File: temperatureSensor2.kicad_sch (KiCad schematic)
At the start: 3 parts, among them J2 Conn_01x03_Pin

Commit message: first draft
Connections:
- net tempSensor1_OUT renamed tempSensor2_OUT
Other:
- note added: "Temperature Sensor 2"
- note removed: "Temperature Sensor 1"

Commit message: revision
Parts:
- added TP2: TestPoint, TestPoint:TestPoint_THTPad_D2.0mm_Drill1.0mm, symbol Connector:TestPoint
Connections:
- net tempSensor2_OUT: now also TP2.1
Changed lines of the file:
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@@
+    )
+  )
+  (symbol (lib_id "Connector:TestPoint") (at 114.3 67.31 0) (unit 1)
+    (in_bom yes) (on_board yes) (dnp no) (fields_autoplaced)
+    (property "Reference" "TP2" (at 116.84 62.738 0)
+      (effects (font (size 1.27 1.27)) (justify left))
+    )
+    (property "Value" "TestPoint" (at 116.84 65.278 0)
+      (effects (font (size 1.27 1.27)) (justify left))
+    )
+    (property "Footprint" "TestPoint:TestPoint_THTPad_D2.0mm_Drill1.0mm" (at 119.38 67.31 0)
+      (effects (font (size 1.27 1.27)) hide)
+    )
+    (property "Datasheet" "~" (at 119.38 67.31 0)
+      (effects (font (size 1.27 1.27)) hide)
+    )
+    (pin "1")
+    (instances
+      (project "Telemetry-Peripheral-SOM-Daughterboard-IMU"
+        (path "/637f68f0-cb9c-412a-8573-5d8e7ef6d8a2/77daee33-11f8-432f-a415-017f7b28dc11"
+          (reference "TP2") (unit 1)
+        )
+      )
     )
   )

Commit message: Integrated changes made by BPS
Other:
- moved on the sheet: C7, C8, J2, TP2

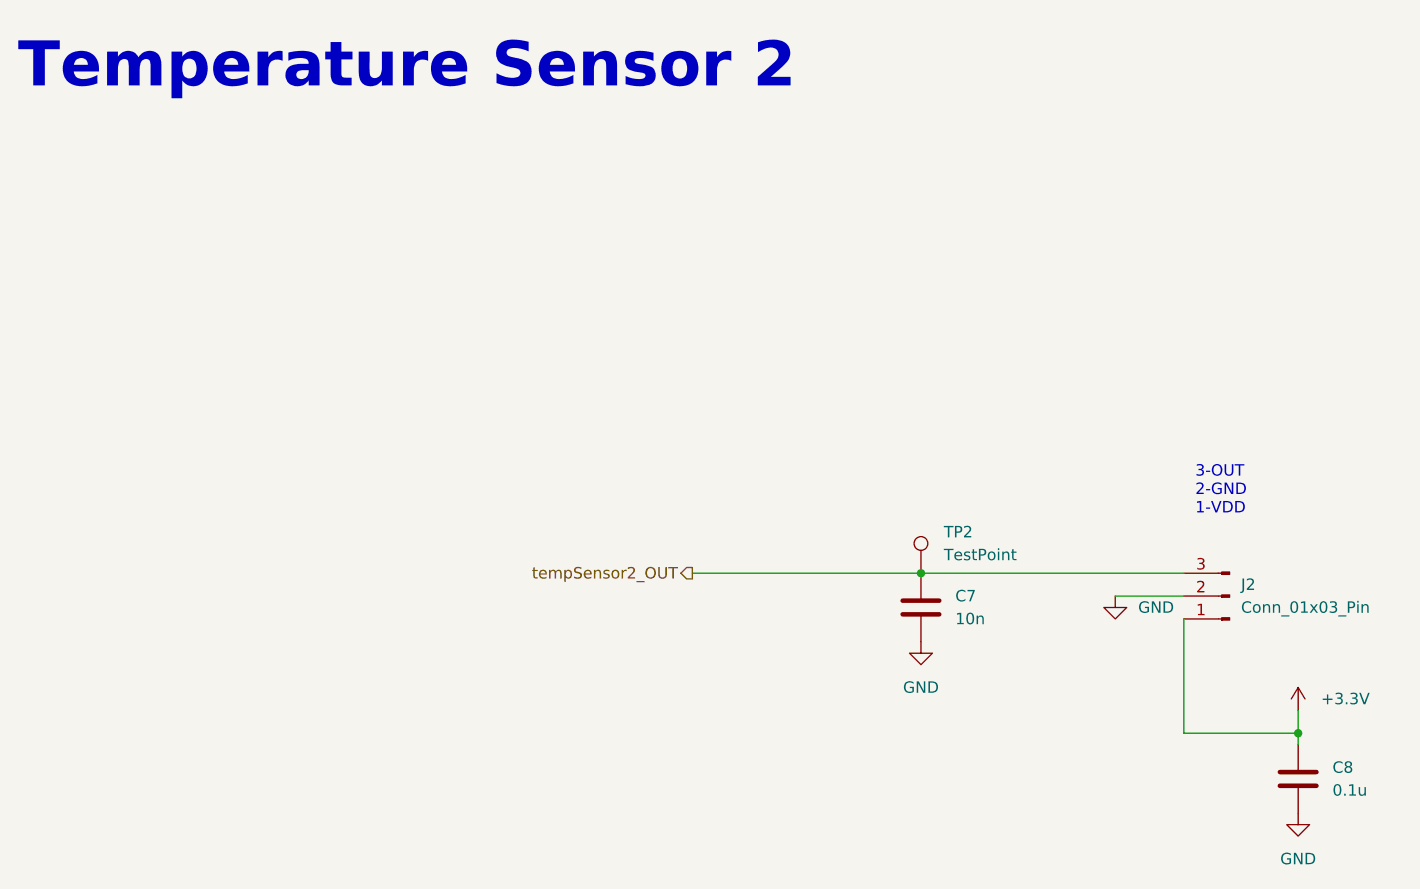
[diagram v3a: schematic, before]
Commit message: added protective circuitry for temp sensors, made name changes for IMU
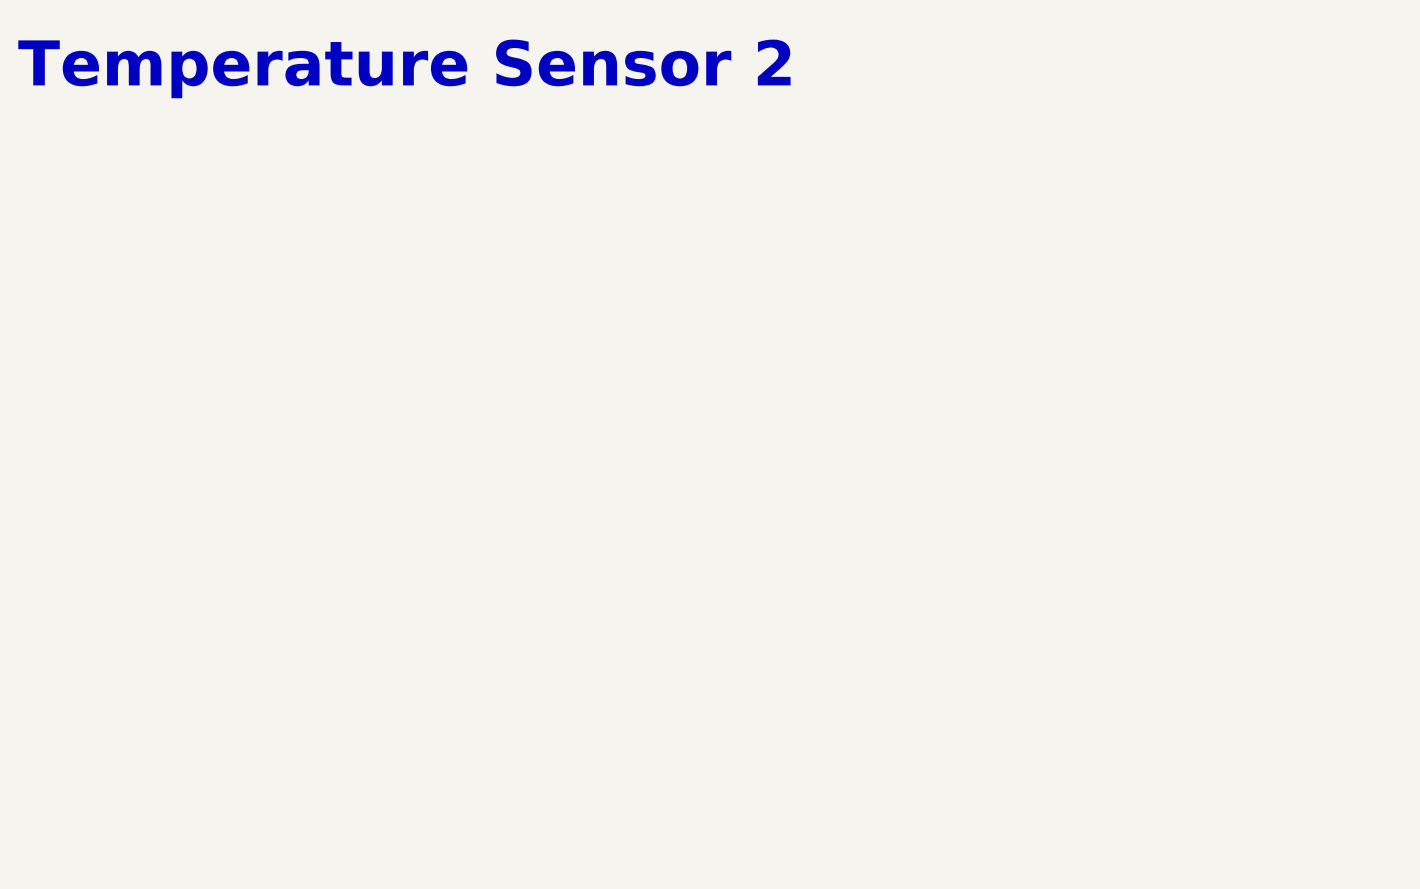
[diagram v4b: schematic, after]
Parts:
- removed C7: 10n, Capacitor_SMD:C_0805_2012Metric, symbol Device:C
- removed C8: 0.1u, Capacitor_SMD:C_0805_2012Metric, symbol Device:C
- removed J2: Conn_01x03_Pin, UTSVT_Connectors:Molex_MicroFit3.0_1x3xP3.00mm_PolarizingPeg_Vertical, symbol Connector:Conn_01x03_Pin
- removed TP2: TestPoint, TestPoint:TestPoint_THTPad_D2.0mm_Drill1.0mm, symbol Connector:TestPoint
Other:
- note removed: "3-OUT 2-GND 1-VDD"
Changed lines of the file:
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@@
 (kicad_sch (version 20230121) (generator eeschema)
   (paper "A4")
-  (junction (at 157.48 92.71) (diameter 0) (color 0 0 0 0)
-  )
-  (junction (at 115.57 74.93) (diameter 0) (color 0 0 0 0)
-  )
-  (wire (pts (xy 115.57 74.93) (xy 144.78 74.93))
-    (stroke (width 0) (type default))
-  )
-  (wire (pts (xy 157.48 92.71) (xy 157.48 93.98))
-    (stroke (width 0) (type default))
-  )
-  (wire (pts (xy 144.78 92.71) (xy 157.48 92.71))
-    (stroke (width 0) (type default))
-  )
-  (wire (pts (xy 157.48 90.17) (xy 157.48 92.71))
-    (stroke (width 0) (type default))
-  )
-  (wire (pts (xy 137.16 77.47) (xy 144.78 77.47))
-    (stroke (width 0) (type default))
-  )
-  (wire (pts (xy 144.78 80.01) (xy 144.78 92.71))
-    (stroke (width 0) (type default))
-  )
-  (wire (pts (xy 90.17 74.93) (xy 115.57 74.93))
-    (stroke (width 0) (type default))
-  )
-  (text "3-OUT\n2-GND\n1-VDD" (at 146.05 68.58 0)
-    (effects (font (size 1.27 1.27)) (justify left bottom))
-  )
   (text "Temperature Sensor 2\n" (at 15.24 21.59 0)
     (effects (font (size 5 5) (thickness 1) bold) (justify left bottom))
   )
-  (hierarchical_label "tempSensor2_OUT" (shape output) (at 90.17 74.93 180) (fields_autoplaced)
-    (effects (font (size 1.27 1.27)) (justify right))
-  )
-  (symbol (lib_id "power:GND") (at 115.57 82.55 0) (unit 1)
-    (in_bom yes) (on_board yes) (dnp no) (fields_autoplaced)
-    (property "Reference" "#PWR017" (at 115.57 88.9 0)
-      (effects (font (size 1.27 1.27)) hide)
-    )
-    (property "Value" "GND" (at 115.57 87.63 0)
-      (effects (font (size 1.27 1.27)))
-    )
-    (property "Footprint" "" (at 115.57 82.55 0)
-      (effects (font (size 1.27 1.27)) hide)
-    )
-    (property "Datasheet" "" (at 115.57 82.55 0)
-      (effects (font (size 1.27 1.27)) hide)
-    )
-    (pin "1")
-    (instances
-      (project "Telemetry-Peripheral-SOM-Daughterboard-IMU"
-        (path "/637f68f0-cb9c-412a-8573-5d8e7ef6d8a2/0366cb5e-31c7-40b1-9d0c-97ad688b48f0"
-          (reference "#PWR017") (unit 1)
-        )
-        (path "/637f68f0-cb9c-412a-8573-5d8e7ef6d8a2/77daee33-11f8-432f-a415-017f7b28dc11"
-          (reference "#PWR04") (unit 1)
-        )
-      )
-    )
-  )
-  (symbol (lib_id "power:GND") (at 157.48 101.6 0) (unit 1)
-    (in_bom yes) (on_board yes) (dnp no) (fields_autoplaced)
-    (property "Reference" "#PWR018" (at 157.48 107.95 0)
-      (effects (font (size 1.27 1.27)) hide)
-    )
-    (property "Value" "GND" (at 157.48 106.68 0)
-      (effects (font (size 1.27 1.27)))
-    )
-    (property "Footprint" "" (at 157.48 101.6 0)
-      (effects (font (size 1.27 1.27)) hide)
-    )
-    (property "Datasheet" "" (at 157.48 101.6 0)
-      (effects (font (size 1.27 1.27)) hide)
-    )
-    (pin "1")
-    (instances
-      (project "Telemetry-Peripheral-SOM-Daughterboard-IMU"
-        (path "/637f68f0-cb9c-412a-8573-5d8e7ef6d8a2/0366cb5e-31c7-40b1-9d0c-97ad688b48f0"
-          (reference "#PWR018") (unit 1)
-        )
-        (path "/637f68f0-cb9c-412a-8573-5d8e7ef6d8a2/77daee33-11f8-432f-a415-017f7b28dc11"
-          (reference "#PWR011") (unit 1)
-        )
-      )
-    )
-  )
-  (symbol (lib_id "Device:C") (at 115.57 78.74 0) (unit 1)
-    (in_bom yes) (on_board yes) (dnp no) (fields_autoplaced)
-    (property "Reference" "C7" (at 119.38 77.47 0)
-      (effects (font (size 1.27 1.27)) (justify left))
-    )
-    (property "Value" "10n" (at 119.38 80.01 0)
-      (effects (font (size 1.27 1.27)) (justify left))
-    )
-    (property "Footprint" "Capacitor_SMD:C_0805_2012Metric" (at 116.5352 82.55 0)
-      (effects (font (size 1.27 1.27)) hide)
-    )
-    (property "Datasheet" "~" (at 115.57 78.74 0)
-      (effects (font (size 1.27 1.27)) hide)
-    )
-    (pin "1")
-    (pin "2")
-    (instances
-      (project "Telemetry-Peripheral-SOM-Daughterboard-IMU"
-        (path "/637f68f0-cb9c-412a-8573-5d8e7ef6d8a2/0366cb5e-31c7-40b1-9d0c-97ad688b48f0"
-          (reference "C7") (unit 1)
-        )
-        (path "/637f68f0-cb9c-412a-8573-5d8e7ef6d8a2/77daee33-11f8-432f-a415-017f7b28dc11"
-          (reference "C9") (unit 1)
-        )
-      )
-    )
-  )
-  (symbol (lib_id "Connector:TestPoint") (at 115.57 74.93 0) (unit 1)
-    (in_bom yes) (on_board yes) (dnp no) (fields_autoplaced)
-    (property "Reference" "TP2" (at 118.11 70.358 0)
-      (effects (font (size 1.27 1.27)) (justify left))
-    )
-    (property "Value" "TestPoint" (at 118.11 72.898 0)
-      (effects (font (size 1.27 1.27)) (justify left))
-    )
-    (property "Footprint" "TestPoint:TestPoint_THTPad_D2.0mm_Drill1.0mm" (at 120.65 74.93 0)
-      (effects (font (size 1.27 1.27)) hide)
-    )
-    (property "Datasheet" "~" (at 120.65 74.93 0)
-      (effects (font (size 1.27 1.27)) hide)
-    )
-    (pin "1")
-    (instances
-      (project "Telemetry-Peripheral-SOM-Daughterboard-IMU"
-        (path "/637f68f0-cb9c-412a-8573-5d8e7ef6d8a2/77daee33-11f8-432f-a415-017f7b28dc11"
-          (reference "TP2") (unit 1)
-        )
-      )
-    )
-  )
-  (symbol (lib_id "power:GND") (at 137.16 77.47 0) (unit 1)
-    (in_bom yes) (on_board yes) (dnp no) (fields_autoplaced)
-    (property "Reference" "#PWR015" (at 137.16 83.82 0)
-      (effects (font (size 1.27 1.27)) hide)
-    )
-    (property "Value" "GND" (at 139.7 78.74 0)
-      (effects (font (size 1.27 1.27)) (justify left))
-    )
-    (property "Footprint" "" (at 137.16 77.47 0)
-      (effects (font (size 1.27 1.27)) hide)
-    )
-    (property "Datasheet" "" (at 137.16 77.47 0)
-      (effects (font (size 1.27 1.27)) hide)
-    )
-    (pin "1")
-    (instances
-      (project "Telemetry-Peripheral-SOM-Daughterboard-IMU"
-        (path "/637f68f0-cb9c-412a-8573-5d8e7ef6d8a2/0366cb5e-31c7-40b1-9d0c-97ad688b48f0"
-          (reference "#PWR015") (unit 1)
-        )
-        (path "/637f68f0-cb9c-412a-8573-5d8e7ef6d8a2/77daee33-11f8-432f-a415-017f7b28dc11"
-          (reference "#PWR05") (unit 1)
-        )
-      )
-    )
-  )
-  (symbol (lib_id "Device:C") (at 157.48 97.79 0) (unit 1)
-    (in_bom yes) (on_board yes) (dnp no) (fields_autoplaced)
-    (property "Reference" "C8" (at 161.29 96.52 0)
-      (effects (font (size 1.27 1.27)) (justify left))
-    )
-    (property "Value" "0.1u" (at 161.29 99.06 0)
-      (effects (font (size 1.27 1.27)) (justify left))
-    )
-    (property "Footprint" "Capacitor_SMD:C_0805_2012Metric" (at 158.4452 101.6 0)
-      (effects (font (size 1.27 1.27)) hide)
-    )
-    (property "Datasheet" "~" (at 157.48 97.79 0)
-      (effects (font (size 1.27 1.27)) hide)
-    )
-    (pin "1")
-    (pin "2")
-    (instances
-      (project "Telemetry-Peripheral-SOM-Daughterboard-IMU"
-        (path "/637f68f0-cb9c-412a-8573-5d8e7ef6d8a2/0366cb5e-31c7-40b1-9d0c-97ad688b48f0"
-          (reference "C8") (unit 1)
-        )
-        (path "/637f68f0-cb9c-412a-8573-5d8e7ef6d8a2/77daee33-11f8-432f-a415-017f7b28dc11"
-          (reference "C10") (unit 1)
-        )
-      )
-    )
-  )
-  (symbol (lib_id "Connector:Conn_01x03_Pin") (at 149.86 77.47 180) (unit 1)
-    (in_bom yes) (on_board yes) (dnp no) (fields_autoplaced)
-    (property "Reference" "J2" (at 151.13 76.2 0)
-      (effects (font (size 1.27 1.27)) (justify right))
-    )
-    (property "Value" "Conn_01x03_Pin" (at 151.13 78.74 0)
-      (effects (font (size 1.27 1.27)) (justify right))
-    )
-    (property "Footprint" "UTSVT_Connectors:Molex_MicroFit3.0_1x3xP3.00mm_PolarizingPeg_Vertical" (at 149.86 77.47 0)
-      (effects (font (size 1.27 1.27)) hide)
-    )
-    (property "Datasheet" "https://www.molex.com/en-us/products/part-detail/436500315?display=pdf" (at 149.86 77.47 0)
-      (effects (font (size 1.27 1.27)) hide)
-    )
-    (pin "1")
-    (pin "2")
-    (pin "3")
-    (instances
-      (project "Telemetry-Peripheral-SOM-Daughterboard-IMU"
-        (path "/637f68f0-cb9c-412a-8573-5d8e7ef6d8a2/0366cb5e-31c7-40b1-9d0c-97ad688b48f0"
-          (reference "J2") (unit 1)
-        )
-        (path "/637f68f0-cb9c-412a-8573-5d8e7ef6d8a2/77daee33-11f8-432f-a415-017f7b28dc11"
-          (reference "J3") (unit 1)
-        )
-      )
-    )
-  )
-  (symbol (lib_id "power:+3.3V") (at 157.48 90.17 0) (unit 1)
-    (in_bom yes) (on_board yes) (dnp no) (fields_autoplaced)
-    (property "Reference" "#PWR016" (at 157.48 93.98 0)
-      (effects (font (size 1.27 1.27)) hide)
-    )
-    (property "Value" "+3.3V" (at 160.02 88.9 0)
-      (effects (font (size 1.27 1.27)) (justify left))
-    )
-    (property "Footprint" "" (at 157.48 90.17 0)
-      (effects (font (size 1.27 1.27)) hide)
-    )
-    (property "Datasheet" "" (at 157.48 90.17 0)
-      (effects (font (size 1.27 1.27)) hide)
-    )
-    (pin "1")
-    (instances
-      (project "Telemetry-Peripheral-SOM-Daughterboard-IMU"
-        (path "/637f68f0-cb9c-412a-8573-5d8e7ef6d8a2/0366cb5e-31c7-40b1-9d0c-97ad688b48f0"
-          (reference "#PWR016") (unit 1)
-        )
-        (path "/637f68f0-cb9c-412a-8573-5d8e7ef6d8a2/77daee33-11f8-432f-a415-017f7b28dc11"
-          (reference "#PWR010") (unit 1)
-        )
-      )
-    )
-  )
 )
